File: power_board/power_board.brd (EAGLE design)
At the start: 68.2 x 78.7 mm, 51 parts, among them IC1 ATTINY24/44/84-PU, Q1 IRL540N, Q2 IRL540N, Q3 IRL540N, Q4 IRL540N, T1 BC337, T2 BC337

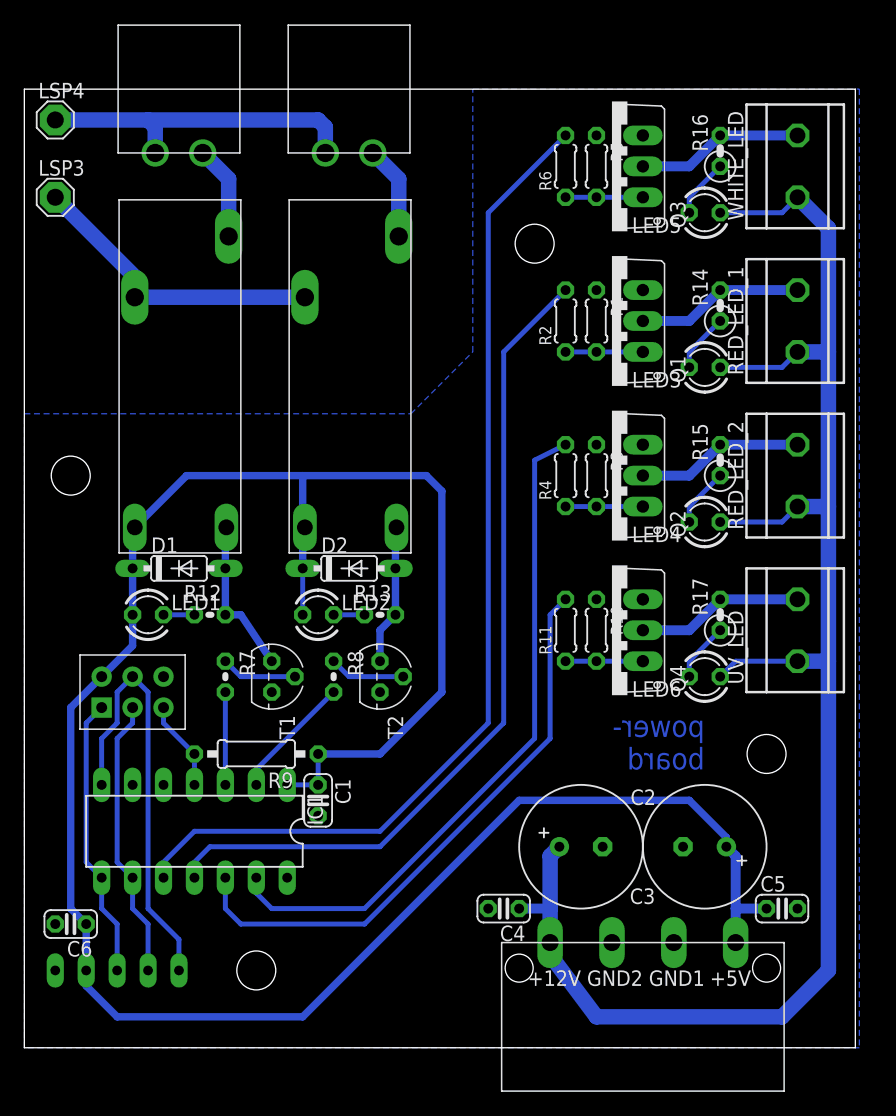
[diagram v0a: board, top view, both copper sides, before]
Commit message: Board-Abmessungen auf gerade Werte gesetzt Beschriftung Befestigung etwas verschoben
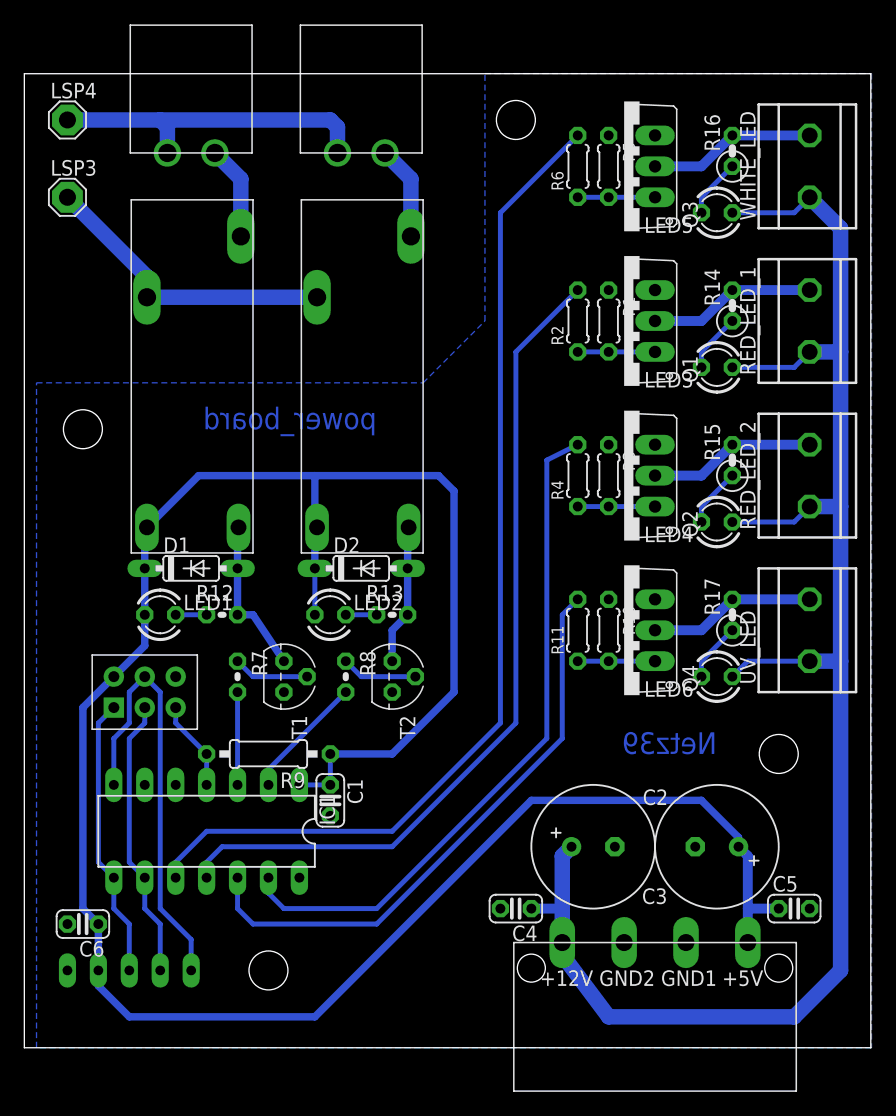
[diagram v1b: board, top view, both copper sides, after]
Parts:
- moved BUBBLES_RELAIS 1.00 mm to (27.7, 78.7)
- moved C1 1.00 mm to (25.1, 20.3)
- moved C2 1.00 mm to (46.7, 16.5)
- moved C3 1.00 mm to (56.9, 16.5)
- moved C4 1.00 mm to (40.4, 11.4)
- moved C5 1.00 mm to (63.2, 11.4)
- moved D1 1.00 mm to (13.7, 39.4)
- moved D2 1.00 mm to (27.7, 39.4)
- moved IC1 1.00 mm to (15.0, 17.8)
- moved LED1 1.00 mm to (11.2, 35.6)
- moved LED2 1.00 mm to (25.1, 35.6)
- moved LED3 1.00 mm to (56.9, 55.9)
- moved LED4 1.00 mm to (56.9, 43.2)
- moved LED5 1.00 mm to (56.9, 68.6)
- moved LED6 1.00 mm to (56.9, 30.5)
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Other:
- board size 68.2 x 78.7 mm -> 69.5 x 80 mm
- board text added: "Netz39"
- board text added: "power_board"
- board text removed: "power- board"
